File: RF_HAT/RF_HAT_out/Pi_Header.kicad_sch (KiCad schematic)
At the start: 1 part, among them J3 Raspberry_Pi_2_3

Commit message: switched to 0603 for all passives
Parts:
- J3: hierarchy_path /03cc9bb1-75ec-4755-9977-259c49401791/96fd858e-f400-4385-b5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 -> /bd07fb41-9ea7-4d0f-b403-cbcdc979b1cd/85b9102e-35b1-4162-ac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; root_uuid 03cc9bb1-75ec-4755-9977-259c49401791 -> bd07fb41-9ea7-4d0f-b403-cbcdc979b1cd
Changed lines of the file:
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@@
+		)
+	)
+	(hierarchical_label "UART_RX"
+		(shape input)
+		(at 30.48 45.72 180)
+		(effects
+			(font
+				(size 1.27 1.27)
+			)
+			(justify right)
 		)
 	)
@@
 		)
 	)
+	(hierarchical_label "GND"
+		(shape input)
+		(at 50.8 99.06 270)
+		(effects
+			(font
+				(size 1.27 1.27)
+			)
+			(justify right)
+		)
+	)
+	(hierarchical_label "VCC_3V3_PI"
+		(shape input)
+		(at 55.88 33.02 90)
+		(effects
+			(font
+				(size 1.27 1.27)
+			)
+			(justify left)
+		)
+	)
+	(hierarchical_label "GND"
+		(shape input)
+		(at 50.8 99.06 270)
+		(effects
+			(font
+				(size 1.27 1.27)
+			)
+			(justify right)
+		)
+	)
+	(hierarchical_label "GND"
+		(shape input)
+		(at 50.8 99.06 270)
+		(effects
+			(font
+				(size 1.27 1.27)
+			)
+			(justify right)
+		)
+	)
+	(hierarchical_label "VCC_3V3_PI"
+		(shape input)
+		(at 55.88 33.02 90)
+		(effects
+			(font
+				(size 1.27 1.27)
+			)
+			(justify left)
+		)
+	)
 	(hierarchical_label "UART_TX"
 		(shape input)
@@
 		)
 	)
-	(hierarchical_label "GND"
-		(shape input)
-		(at 50.8 99.06 270)
-		(effects
-			(font
-				(size 1.27 1.27)
-			)
-			(justify right)
-		)
-	)
-	(hierarchical_label "GND"
-		(shape input)
-		(at 50.8 99.06 270)
-		(effects
-			(font
-				(size 1.27 1.27)
-			)
-			(justify right)
-		)
-	)
-	(hierarchical_label "GND"
-		(shape input)
-		(at 50.8 99.06 270)
-		(effects
-			(font
-				(size 1.27 1.27)
-			)
-			(justify right)
-		)
-	)
-	(hierarchical_label "VCC_3V3_PI"
-		(shape input)
-		(at 55.88 33.02 90)
+	(hierarchical_label "+5V"
+		(shape input)
+		(at 45.72 33.02 90)
 		(effects
 			(font
@@
 		)
 	)
-	(hierarchical_label "VCC_3V3_PI"
-		(shape input)
-		(at 55.88 33.02 90)
-		(effects
-			(font
-				(size 1.27 1.27)
-			)
-			(justify left)
-		)
-	)
-	(hierarchical_label "GND"
-		(shape input)
-		(at 50.8 99.06 270)
-		(effects
-			(font
-				(size 1.27 1.27)
-			)
-			(justify right)
-		)
-	)
-	(hierarchical_label "UART_RX"
-		(shape input)
-		(at 30.48 45.72 180)
-		(effects
-			(font
-				(size 1.27 1.27)
-			)
-			(justify right)
-		)
-	)
-	(hierarchical_label "+5V"
-		(shape input)
-		(at 45.72 33.02 90)
-		(effects
-			(font
-				(size 1.27 1.27)
-			)
-			(justify left)
+	(hierarchical_label "GND"
+		(shape input)
+		(at 50.8 99.06 270)
+		(effects
+			(font
+				(size 1.27 1.27)
+			)
+			(justify right)
 		)
 	)
@@
 			)
 		)
-		(property "hierarchy_path" "/03cc9bb1-75ec-4755-9977-259c49401791/96fd858e-f400-4385-b5e2-13759435a1c9"
+		(property "hierarchy_path" "/bd07fb41-9ea7-4d0f-b403-cbcdc979b1cd/85b9102e-35b1-4162-acd5-8bc3feeafeb6"
 			(at 53.34 71.1199 0)
 			(effects
@@
 			)
 		)
-		(property "root_uuid" "03cc9bb1-75ec-4755-9977-259c49401791"
+		(property "root_uuid" "bd07fb41-9ea7-4d0f-b403-cbcdc979b1cd"
 			(at 53.34 71.1199 0)
 			(effects
@@
 		(instances
 			(project ""
-				(path "/03cc9bb1-75ec-4755-9977-259c49401791/96fd858e-f400-4385-b5e2-13759435a1c9"
+				(path "/bd07fb41-9ea7-4d0f-b403-cbcdc979b1cd/85b9102e-35b1-4162-acd5-8bc3feeafeb6"
 					(reference "J3")
 					(unit 1)

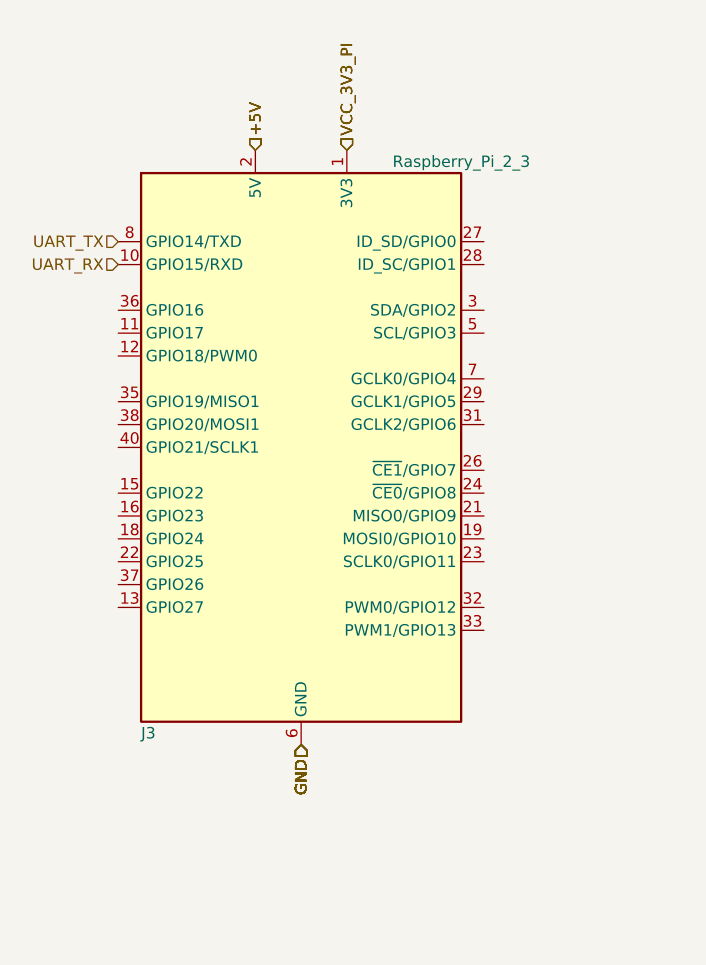
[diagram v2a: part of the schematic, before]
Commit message: Restructured kicad schematic for CC1200 PI_HAT readablitity based on M17 reference schematics
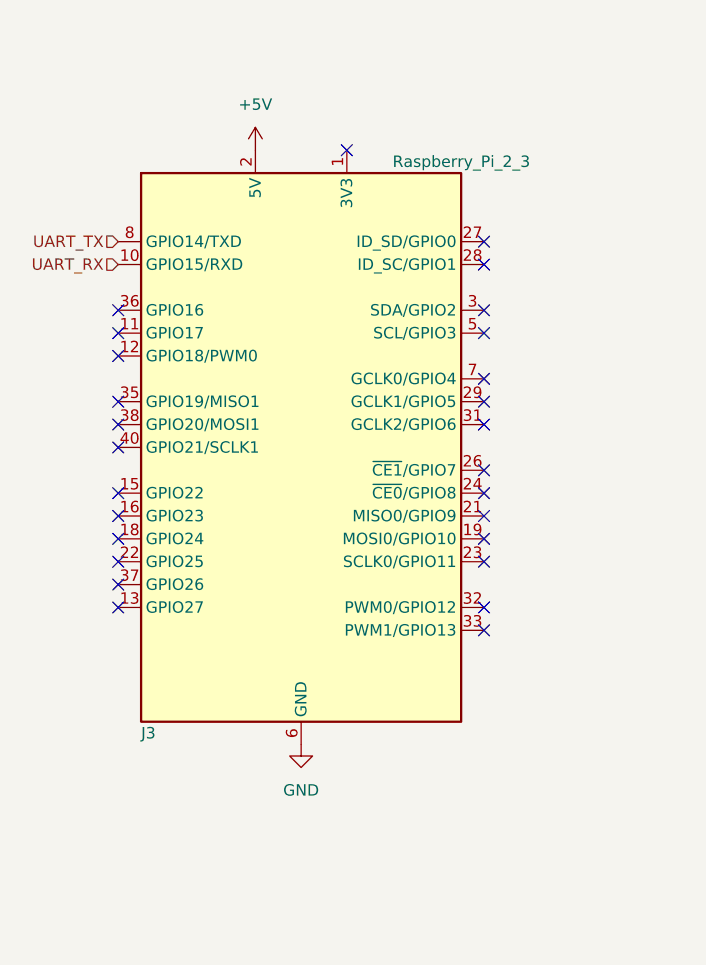
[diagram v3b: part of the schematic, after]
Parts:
- J3: hierarchy_path /bd07fb41-9ea7-4d0f-b403-cbcdc979b1cd/85b9102e-35b1-4162-ac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 -> /300cf3d4-e317-44c8-acd8-5f9989779c7c/df2c4ae5-dfcc-4b06-a5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; root_uuid bd07fb41-9ea7-4d0f-b403-cbcdc979b1cd -> 300cf3d4-e317-44c8-acd8-5f9989779c7c
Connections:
- net VCC_3V3_PI: no longer names the net of J3.1 (3V3), J3.17 (3V3)
- no-connect marks 0 -> 27

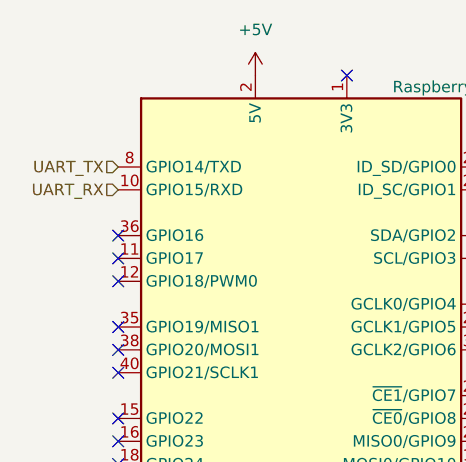
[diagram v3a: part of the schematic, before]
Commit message: fixed schematic and updated readme's
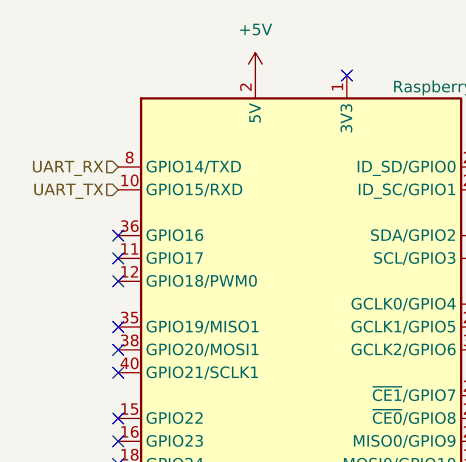
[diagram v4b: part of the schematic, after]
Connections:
- net UART_RX: now also J3.8 (GPIO14/TXD); no longer J3.10 (GPIO15/RXD)
- net UART_TX: now also J3.10 (GPIO15/RXD); no longer J3.8 (GPIO14/TXD)
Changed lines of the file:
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@@
 	(hierarchical_label "UART_RX"
 		(shape input)
-		(at 30.48 45.72 180)
+		(at 30.48 43.18 180)
 		(effects
 			(font
@@
 	(hierarchical_label "UART_TX"
 		(shape input)
-		(at 30.48 43.18 180)
+		(at 30.48 45.72 180)
 		(effects
 			(font

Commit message: did final routing and added Farnell and LCSC numbers to all components
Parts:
- J3: Farnell (none) -> 9838309; LCSC (none) -> C50980
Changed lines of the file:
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@@
+			)
+		)
+		(property "Farnell" "9838309"
+			(at 50.8 66.04 0)
+			(effects
+				(font
+					(size 1.27 1.27)
+				)
+				(hide yes)
+			)
+		)
+		(property "LCSC" "C50980"
+			(at 50.8 66.04 0)
+			(effects
+				(font
+					(size 1.27 1.27)
+				)
+				(hide yes)
 			)
 		)
